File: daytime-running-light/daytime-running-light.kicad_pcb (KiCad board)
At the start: 2 copper layers, 47 parts, among them J1 Conn_01x01_Socket, J2 Conn_01x01_Socket, J3 Conn_01x01_Socket, J4 Conn_01x02_Socket, Q1 2N3904, Q2 2N3904, Q3 IRFZ44N, Q4 IRF9321, SW1 SW_SPST, SW2 SW_SPST, U1 L7812, U2 4069, U3 4001

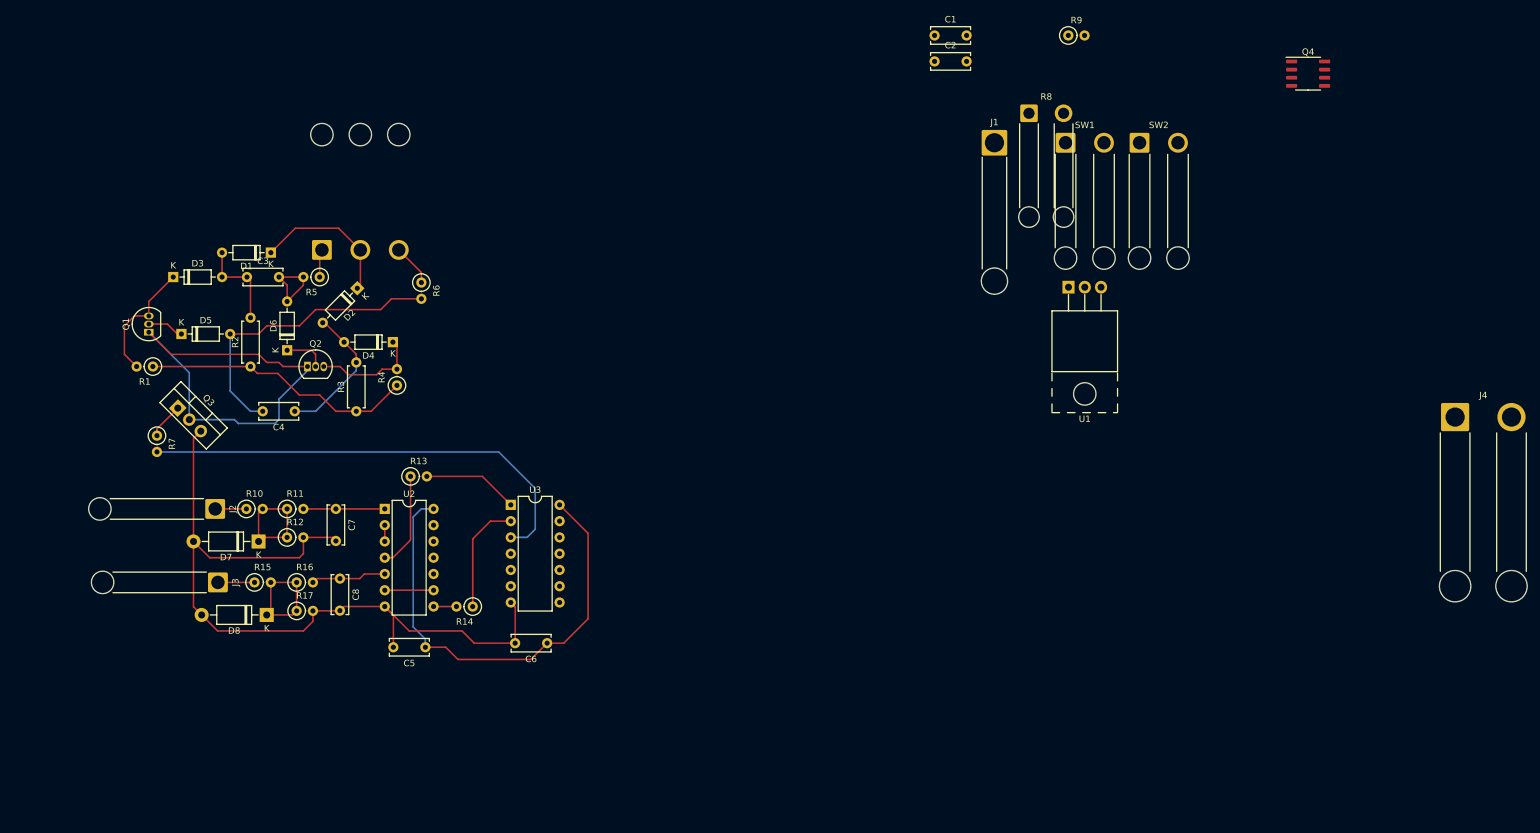
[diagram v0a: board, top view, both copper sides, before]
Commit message: [drl] Change daytime running light to use TLC555 timer.
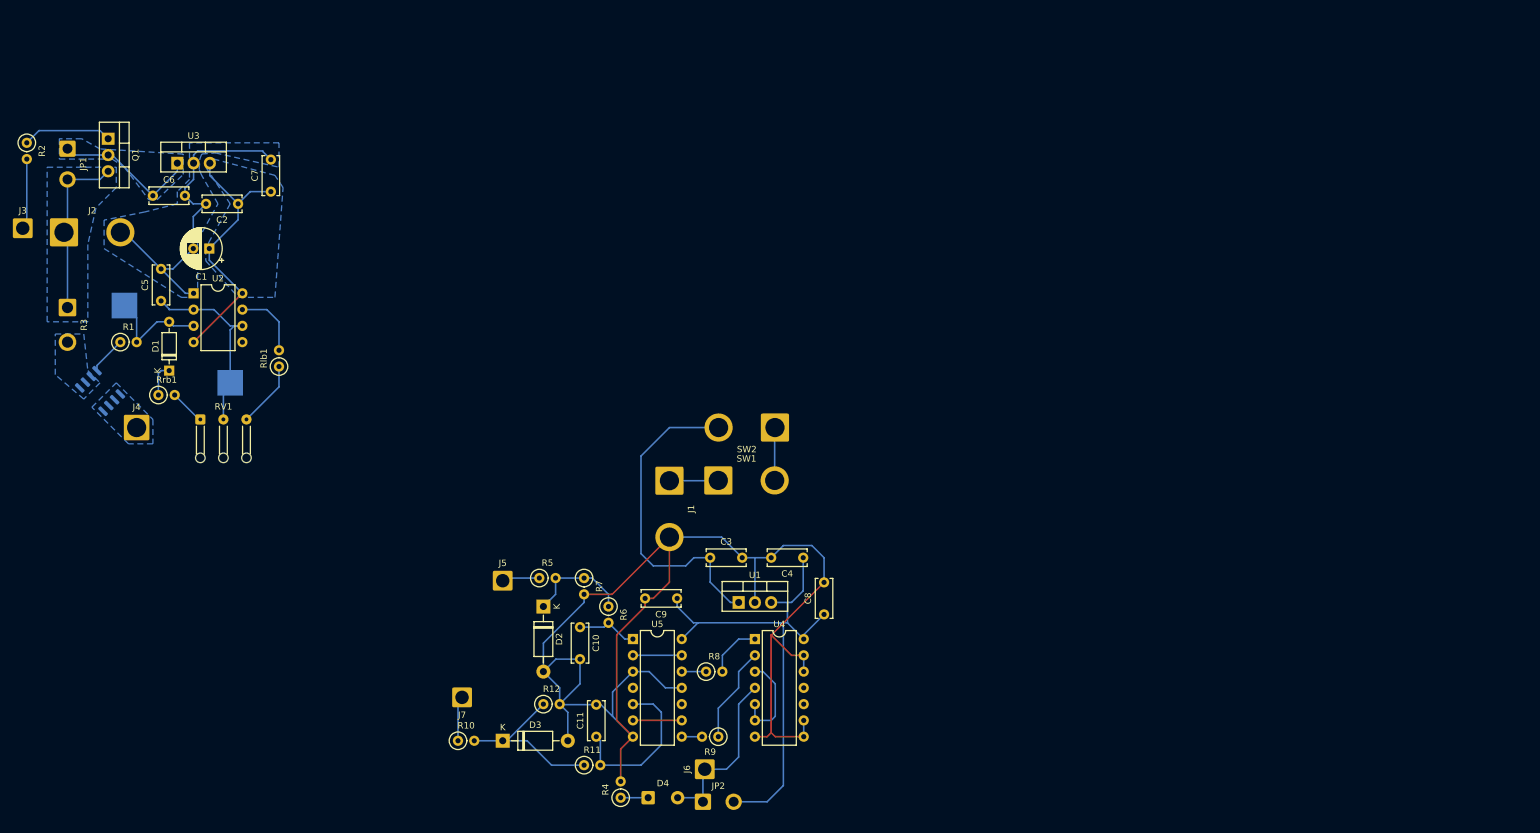
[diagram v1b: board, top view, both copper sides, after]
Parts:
- removed D5, D6: 1N4148, Diode_THT:D_DO-35_SOD27_P7.62mm_Horizontal
- removed D7: 1N47xxA, Diode_THT:D_DO-41_SOD81_P10.16mm_Horizontal
- removed D8: 1N4742A, Diode_THT:D_DO-41_SOD81_P10.16mm_Horizontal
- removed Q3: IRFZ44N, Package_TO_SOT_THT:TO-220-3_Vertical
- removed Q4: IRF9321, LIB:SO-8_3.9x4.9mm_P1.27mm
- removed R13, R14, R15: 1k, Resistor_THT:R_Axial_DIN0207_L6.3mm_D2.5mm_P2.54mm_Vertical
- removed R16: 47k, Resistor_THT:R_Axial_DIN0207_L6.3mm_D2.5mm_P2.54mm_Vertical
- removed R17: 100k, Resistor_THT:R_Axial_DIN0207_L6.3mm_D2.5mm_P2.54mm_Vertical
- added C10: 0.33uF, Capacitor_THT:C_Disc_D6.0mm_W2.5mm_P5.00mm, F.Cu at (127.0, 122.0)
- added C11: 0.33uF, Capacitor_THT:C_Disc_D6.0mm_W2.5mm_P5.00mm, F.Cu at (129.5, 139.1)
- added C9: 0.1uF, Capacitor_THT:C_Disc_D6.0mm_W2.5mm_P5.00mm, F.Cu at (142.2, 117.5)
- added J5: Conn_01x01_Socket, Connector_Wire:SolderWire-1.5sqmm_1x01_D1.7mm_OD3mm, F.Cu at (114.9, 114.7)
- added J6: Conn_01x01_Pin, Connector_Wire:SolderWire-1.5sqmm_1x01_D1.7mm_OD3mm, F.Cu at (146.5, 144.1)
- added J7: Conn_01x01_Socket, Connector_Wire:SolderWire-1.5sqmm_1x01_D1.7mm_OD3mm, F.Cu at (108.6, 132.9)
- added JP1: Jumper_2_Open, Connector_Wire:SolderWire-0.75sqmm_1x02_P4.8mm_D1.25mm_OD2.3mm, F.Cu at (47.0, 47.3)
- added JP2: Jumper_2_Open, Connector_Wire:SolderWire-0.75sqmm_1x02_P4.8mm_D1.25mm_OD2.3mm, F.Cu at (146.2, 149.2)
- added Rlb1: 1k, Resistor_THT:R_Axial_DIN0207_L6.3mm_D2.5mm_P2.54mm_Vertical, F.Cu at (80.0, 81.3)
- added Rrb1: 1k, Resistor_THT:R_Axial_DIN0207_L6.3mm_D2.5mm_P2.54mm_Vertical, F.Cu at (61.2, 85.7)
- added TPpwm1: TestPoint, TestPoint:TestPoint_Pad_4.0x4.0mm, B.Cu at (55.9, 71.8)
- added TPpwmC1: TestPoint, TestPoint:TestPoint_Pad_4.0x4.0mm, B.Cu at (72.4, 83.8)
- added U4: 4001, Package_DIP:DIP-14_W7.62mm, F.Cu at (154.3, 123.8)
- added U5: 4069, Package_DIP:DIP-14_W7.62mm, F.Cu at (135.3, 123.8)
- C1: value 0.33uF -> 2u; footprint Capacitor_THT:C_Disc_D6.0mm_W2.5mm_P5.00mm -> Capacitor_THT:CP_Radial_D6.3mm_P2.50mm
- C2: value 0.1uF -> 0.1u
- C3: value 10nF -> 0.33uF
- C4: value 10nF -> 0.1uF
- C5: value 0.1uF -> 33n
- C6: value 0.1uF -> 0.33uF
- C7, C8: value 0.33uF -> 0.1uF
- D1: value 1N4148 -> BAT42
- D2: value 1N4148 -> 1N47xxA; footprint Diode_THT:D_DO-35_SOD27_P7.62mm_Horizontal -> Diode_THT:D_DO-41_SOD81_P10.16mm_Horizontal
- D3: value 1N4148 -> 1N4742A; footprint Diode_THT:D_DO-35_SOD27_P7.62mm_Horizontal -> Diode_THT:D_DO-41_SOD81_P10.16mm_Horizontal
- D4: value 1N4148 -> LED; footprint Diode_THT:D_DO-35_SOD27_P7.62mm_Horizontal -> Connector_Wire:SolderWire-0.5sqmm_1x02_P4.6mm_D0.9mm_OD2.1mm
- J1: value Conn_01x01_Socket -> Conn_01x02_Socket; footprint Connector_Wire:SolderWire-2.5sqmm_1x01_D2.4mm_OD3.6mm_Relief -> Connector_Wire:SolderWire-2.5sqmm_1x02_P8.8mm_D2.4mm_OD4.4mm
- J2: value Conn_01x01_Socket -> Conn_01x02_Socket; footprint Connector_Wire:SolderWire-1.5sqmm_1x01_D1.7mm_OD3mm_Relief -> Connector_Wire:SolderWire-2.5sqmm_1x02_P8.8mm_D2.4mm_OD4.4mm
- J3: footprint Connector_Wire:SolderWire-1.5sqmm_1x01_D1.7mm_OD3mm_Relief -> Connector_Wire:SolderWire-1.5sqmm_1x01_D1.7mm_OD3mm
- J4: value Conn_01x02_Socket -> Conn_01x01_Socket; footprint Connector_Wire:SolderWire-2.5sqmm_1x02_P8.8mm_D2.4mm_OD4.4mm_Relief -> Connector_Wire:SolderWire-2.5sqmm_1x01_D2.4mm_OD3.6mm
- Q1: value 2N3904 -> IRF9540N; footprint Package_TO_SOT_THT:TO-92_Inline -> Package_TO_SOT_THT:TO-220-3_Vertical
- Q2: value 2N3904 -> IRF9321; footprint Package_TO_SOT_THT:TO-92_Inline -> LIB:SO-8_3.9x4.9mm_P1.27mm; moved to B.Cu
- R1: value 3.9k -> 100..1k
- R2: value 3.9k -> 100; footprint Resistor_THT:R_Axial_DIN0207_L6.3mm_D2.5mm_P7.62mm_Horizontal -> Resistor_THT:R_Axial_DIN0207_L6.3mm_D2.5mm_P2.54mm_Vertical
- R3: value 3.9k -> 0.2; footprint Resistor_THT:R_Axial_DIN0207_L6.3mm_D2.5mm_P7.62mm_Horizontal -> Connector_Wire:SolderWire-1sqmm_1x02_P5.4mm_D1.4mm_OD2.7mm
- R4: value 3.9k -> R
- R6: value 1k -> 47k
- R7: value 100 -> 100k
- R8: value 0.2 -> 1k; footprint Connector_Wire:SolderWire-1sqmm_1x02_P5.4mm_D1.4mm_OD2.7mm_Relief -> Resistor_THT:R_Axial_DIN0207_L6.3mm_D2.5mm_P2.54mm_Vertical
- R9: value 100 -> 1k
- RV1: value 100k -> R_Potentiometer; footprint Connector_Wire:SolderWire-1.5sqmm_1x03_P6mm_D1.7mm_OD3mm_Relief -> Connector_Wire:SolderWire-0.1sqmm_1x03_P3.6mm_D0.4mm_OD1mm_Relief; moved to F.Cu
- SW1, SW2: footprint Connector_Wire:SolderWire-1.5sqmm_1x02_P6mm_D1.7mm_OD3mm_Relief -> Connector_Wire:SolderWire-2.5sqmm_1x02_P8.8mm_D2.4mm_OD4.4mm
- U1: footprint Package_TO_SOT_THT:TO-220-3_Horizontal_TabUp -> Package_TO_SOT_THT:TO-220-3_Vertical
- U2: value 4069 -> NE555; footprint Package_DIP:DIP-14_W7.62mm -> Package_DIP:DIP-8_W7.62mm
- U3: value 4001 -> L7812; footprint Package_DIP:DIP-14_W7.62mm -> Package_TO_SOT_THT:TO-220-3_Vertical
- moved J4 205.8 mm to (57.8, 90.8)
- moved R9 122.3 mm to (148.6, 139.1), turned to 180 degrees
- moved C1 118.0 mm to (69.1, 62.9), turned to 180 degrees
- moved C2 111.0 mm to (73.6, 55.9), turned to 180 degrees
- moved R8 100.7 mm to (146.7, 128.9)
- moved C6 93.1 mm to (60.3, 54.6), turned to 0 degrees
- moved D3 88.8 mm to (114.9, 139.7)
- moved C3 84.5 mm to (147.3, 111.1)
- moved C4 82.6 mm to (161.8, 111.1)
- moved D4 81.5 mm to (137.6, 148.6), turned to 0 degrees
- moved C8 75.8 mm to (165.1, 120.0), turned to 90 degrees
- moved SW1 75.6 mm to (148.6, 99.1)
- moved U3 74.5 mm to (64.1, 49.5)
- moved R4 73.2 mm to (133.3, 148.6)
- moved J1 73.2 mm to (141.0, 99.1), turned to -90 degrees
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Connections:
- C1 pad 1: Net-(SW2-B) -> /VCC_STAB2
- C1 pad 2: GND -> GND2
- C2 pad 1: /VCC_STAB -> /VCC_STAB2
- C2 pad 2: GND -> GND2
- C3 pad 1: Net-(D1-A) -> Net-(SW2-B)
- C3 pad 2: Net-(D6-A) -> GND
- C4 pad 1: Net-(D2-A) -> /VCC_STAB
- C4 pad 2: Net-(D5-A) -> GND
- C5 pad 1: /VCC_STAB -> /U1_TR
- C5 pad 2: GND -> GND2
- C6 pad 1: /VCC_STAB -> Net-(JP1-A)
- C6 pad 2: GND -> GND2
- C7 pad 1: Net-(C7-Pad1) -> /VCC_STAB2
- C7 pad 2: GND -> GND2
- C8 pad 1: Net-(C8-Pad1) -> /VCC_STAB
- D2 pad 1: Net-(D1-K) -> Net-(D2-K)
- D2 pad 2: Net-(D2-A) -> GND
- D3 pad 1: /POWER_CONTROL -> Net-(D3-K)
- D3 pad 2: Net-(D1-A) -> GND
- D4 pad 2: Net-(D2-A) -> Net-(D4-A)
- J1 pad 1: Net-(J1-Pin_1) -> VCC
- J2 pad 1: /HEADLIGHT -> +12V
- J3 pad 1: /HIGHBEAM -> Net-(J3-Pin_1)
- J4 pad 1: VCC -> Net-(J4-Pin_1)
- Q1 pad 1: Net-(Q1-E) -> Net-(Q1-G)
- Q1 pad 2: Net-(D5-K) -> Net-(JP1-A)
- Q1 pad 3: /POWER_CONTROL -> +12V
- Q2 pad 1: Net-(Q1-E) -> Net-(J4-Pin_1)
- Q2 pad 2: Net-(D6-K) -> /POWER_CONTROL
- Q2 pad 3: Net-(D4-K) -> Net-(Q2-S)
- R1 pad 1: /VCC_STAB -> /POWER_CONTROL
- R1 pad 2: /POWER_CONTROL -> Net-(D1-A)
- R10 pad 1: /HEADLIGHT -> /HIGHBEAM
- R10 pad 2: Net-(D7-K) -> Net-(D3-K)
- R11 pad 1: Net-(D7-K) -> Net-(D3-K)
- R11 pad 2: Net-(C7-Pad1) -> Net-(C11-Pad1)
- R12 pad 1: Net-(D7-K) -> Net-(D3-K)
- R2 pad 1: /VCC_STAB -> Net-(Q1-G)
- R2 pad 2: Net-(D1-A) -> Net-(J3-Pin_1)
- R3 pad 1: /VCC_STAB -> +12V
- R3 pad 2: Net-(D2-A) -> Net-(Q2-S)
- R4 pad 1: /VCC_STAB -> Net-(D4-K)
- R4 pad 2: Net-(D4-K) -> GND
- R5 pad 1: Net-(R5-Pad1) -> /HEADLIGHT
- R5 pad 2: Net-(D6-A) -> Net-(D2-K)
- R6 pad 1: Net-(R6-Pad1) -> Net-(D2-K)
- R6 pad 2: Net-(D5-A) -> Net-(C10-Pad1)
- R7 pad 1: Net-(Q3-Pad1) -> Net-(D2-K)
- R7 pad 2: /ALLOW_POWER -> GND
- R8 pad 1: VCC -> Net-(R8-Pad1)
- R9 pad 1: /POWER_CONTROL -> Net-(R9-Pad1)
- RV1 pad 1: Net-(R5-Pad1) -> Net-(RV1-Pad1)
- RV1 pad 2: Net-(D1-K) -> /U1_TR
- RV1 pad 3: Net-(R6-Pad1) -> Net-(RV1-Pad3)
- U2 pad 1: Net-(C7-Pad1) -> GND2
- U2 pad 2: Net-(U2-Pad2) -> /U1_TR
- U2 pad 3: Net-(U2-Pad2) -> Net-(D1-A)
- U2 pad 4: Net-(R13-Pad1) -> /VCC_STAB2
- U2 pad 5: Net-(C8-Pad1) -> unconnected-(U2-CV-Pad5)
- U2 pad 6: Net-(U2-Pad6) -> /U1_TR
- U2 pad 7: GND -> /U1_DISCH
- U2 pad 8: Net-(R14-Pad2) -> /VCC_STAB2
- U3 pad 1: Net-(R13-Pad2) -> Net-(JP1-A)
- U3 pad 2: Net-(R14-Pad1) -> GND2
- U3 pad 3: /ALLOW_POWER -> /VCC_STAB2
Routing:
- net GND: track 124.4 -> 218.0 mm
- net /ALLOW_POWER: track 72.1 -> 0.00 mm
- net Net-(Q1-E): track 67.9 -> 0.00 mm
- net GND2: track 0.00 -> 53.2 mm
- net Net-(SW2-B): track 0.00 -> 50.9 mm
- net Net-(D5-A): track 47.4 -> 0.00 mm
- net /VCC_STAB2: track 0.00 -> 42.8 mm
- net /VCC_STAB: track 115.9 -> 80.5 mm
- net /U1_TR: track 0.00 -> 30.9 mm
- net Net-(D3-K): track 0.00 -> 27.4 mm
- net Net-(D4-A): track 0.00 -> 27.3 mm
- net +12V: track 0.00 -> 27.3 mm
- net Net-(C11-Pad1): track 0.00 -> 25.6 mm
- net Net-(JP1-A): track 0.00 -> 23.0 mm
- net Net-(D2-A): track 22.0 -> 0.00 mm
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- added copper zone on B.Cu, net +12V
- added copper zone on B.Cu, net /VCC_STAB2
- added copper zone on B.Cu, net GND2
- added copper zone on B.Cu, net Net-(J4-Pin_1)
- added copper zone on B.Cu, net Net-(JP1-A)
- added copper zone on B.Cu, net Net-(Q2-S)

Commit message: [drl] Update
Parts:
- moved SW2 30.5 mm to (134.1, 110.5), turned to 0 degrees
- moved J1 10.8 mm to (150.5, 104.1), turned to 0 degrees
- moved R5 10.4 mm to (114.3, 122.6)
- moved R10 9.44 mm to (114.9, 133.3), turned to -90 degrees
- moved J7 7.52 mm to (114.9, 128.9)
- moved SW1 6.82 mm to (143.4, 103.5), turned to 180 degrees
- moved R7 4.49 mm to (127.0, 118.7), turned to 90 degrees
- moved J5 2.76 mm to (114.9, 117.5)
- moved R6 0.90 mm to (132.1, 119.4)
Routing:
- net GND: track 218.0 -> 68.8 mm, vias 0 -> 4
- net /VCC_STAB: track 80.5 -> 42.1 mm, vias 0 -> 2
- net Net-(SW2-B): track 50.9 -> 14.3 mm
- net /U1_TR: track 30.9 -> 1.58 mm
- net Net-(U4-Pad3): track 14.6 -> 18.0 mm
- net /HIGHBEAM: track 7.04 -> 4.44 mm
- net Net-(C11-Pad1): track 25.6 -> 26.7 mm
- net Net-(SW1-B): track 6.37 -> 7.21 mm
- net Net-(D3-K): track 27.4 -> 26.8 mm
- net Net-(D2-K): track 16.4 -> 17.1 mm
- net /HEADLIGHT: track 5.89 -> 5.34 mm
- net Net-(C10-Pad1): track 9.59 -> 9.07 mm
- added copper zone on B.Cu, net /U1_TR
- added copper zone on B.Cu, net /VCC_STAB
- added copper zone on B.Cu, net GND

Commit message: [drl] Change schematic and PCB
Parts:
- added D5: 1.5KExxA, Diode_THT:D_DO-201AE_P15.24mm_Horizontal, F.Cu at (51.4, 98.4)
- added D6: 1N4148, Diode_THT:D_DO-35_SOD27_P7.62mm_Horizontal, F.Cu at (54.6, 88.9)
- added Q3: BC548, LIB:TO-92_HandSolder2, F.Cu at (72.4, 55.2)
- added Q4: BC548, LIB:TO-92_HandSolder2, F.Cu at (57.1, 72.4)
- added Q5: BC548, Package_TO_SOT_THT:TO-92_HandSolder, F.Cu at (61.0, 82.9)
- added R13: 100, Resistor_THT:R_Axial_DIN0207_L6.3mm_D2.5mm_P2.54mm_Vertical, F.Cu at (150.9, 144.1)
- added R14: 10k..100k, Resistor_THT:R_Axial_DIN0207_L6.3mm_D2.5mm_P2.54mm_Vertical, F.Cu at (76.2, 50.2)
- added R15: 10k..100k, Resistor_THT:R_Axial_DIN0207_L6.3mm_D2.5mm_P2.54mm_Vertical, F.Cu at (52.2, 76.4)
- added R16: 100, Resistor_THT:R_Axial_DIN0207_L6.3mm_D2.5mm_P2.54mm_Vertical, F.Cu at (58.6, 76.4)
- added R17: 10k, Resistor_THT:R_Axial_DIN0207_L6.3mm_D2.5mm_P2.54mm_Vertical, F.Cu at (55.9, 84.5)
- C1: value 2u -> 0.1u
- Q1, U3: footprint Package_TO_SOT_THT:TO-220-3_Vertical -> LIB:TO-220-3_Vertical-mod
- R1: value 100..1k -> 10k
- R2: value 100 -> 10k
- RV1: value R_Potentiometer -> 51k
- Rlb1: value 1k -> 51k
- U2: value NE555 -> TLC555xP
- moved J3 33.0 mm to (69.8, 45.7)
- moved C6 32.3 mm to (92.1, 48.9), turned to 180 degrees
- moved U3 28.5 mm to (92.1, 54.6), turned to -90 degrees
- moved R2 23.2 mm to (63.7, 48.3), turned to 0 degrees
- moved TPpwm1 22.5 mm to (73.0, 86.4)
- moved C7 17.5 mm to (92.1, 65.4), turned to 180 degrees
- moved RV1 15.2 mm to (79.8, 80.4)
- moved R3 15.1 mm to (49.0, 87.0)
- moved Q2 14.8 mm to (59.7, 97.8), turned to 0 degrees
- moved Rrb1 14.0 mm to (74.1, 80.2)
- moved TPpwmC1 14.0 mm to (83.2, 92.7)
- moved C1 13.7 mm to (82.5, 60.3)
- moved C2 10.9 mm to (83.8, 52.1)
- moved J4 10.3 mm to (67.9, 92.7)
- moved Q1 9.92 mm to (60.4, 52.7)
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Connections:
- net Net-(Q1-G) renamed /ALLOW_POWER_ON
- D1 pad 2: Net-(D1-A) -> /POWER_CONTROL
- J6 pad 1: Net-(D4-A) -> Net-(J6-Pin_1)
- Q2 pad 2: /POWER_CONTROL -> Net-(D6-A)
- R1 pad 1: /POWER_CONTROL -> Net-(Q4-B)
- R1 pad 2: Net-(D1-A) -> /POWER_CONTROL
- TPpwm1 pad 1: Net-(D1-A) -> /POWER_CONTROL
- U2 pad 3: Net-(D1-A) -> /POWER_CONTROL
- U2 pad 4: /VCC_STAB2 -> Net-(Q3-C)
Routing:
- net GND2: track 53.2 -> 11.9 mm
- net Net-(JP1-A): track 23.0 -> 63.8 mm
- net /U1_TR: track 1.58 -> 38.1 mm
- net +12V: track 27.3 -> 2.01 mm
- net Net-(Q3-C): track 0.00 -> 25.2 mm
- net Net-(D6-K): track 0.00 -> 21.8 mm
- net Net-(D5-A1): track 0.00 -> 19.9 mm
- net GND: track 68.8 -> 88.0 mm, vias 4 -> 2
- net Net-(D6-A): track 0.00 -> 17.5 mm
- net Net-(D1-A): track 17.0 -> 0.00 mm
- net Net-(SW2-B): track 14.3 -> 0.90 mm
- net /POWER_CONTROL_INV: track 0.00 -> 8.36 mm
- net VCC: track 7.34 -> 0.90 mm
- net Net-(SW1-B): track 7.21 -> 0.77 mm
- net Net-(J3-Pin_1): track 11.1 -> 4.64 mm
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- added copper zone on B.Cu, net /POWER_CONTROL
- added copper zone on B.Cu, net Net-(SW1-B)
- added copper zone on B.Cu, net Net-(SW2-B)
- added copper zone on B.Cu, net VCC
- removed copper zone on B.Cu, net /U1_TR
- removed copper zone on B.Cu, net /VCC_STAB2
- removed copper zone on B.Cu, net Net-(JP1-A)
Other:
- board outline added: 130.2 x 112.4 mm

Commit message: [drl] Change schematic and PCB
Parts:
- added R18: R, Resistor_THT:R_Axial_DIN0207_L6.3mm_D2.5mm_P2.54mm_Vertical, F.Cu at (141.0, 148.6)
- moved R4 32.4 mm to (165.7, 148.4)
- moved D4 23.2 mm to (160.8, 148.6), turned to 180 degrees
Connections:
- JP2 pad 1: Net-(D4-A) -> Net-(JP2-A)
- JP2 pad 2: /VCC_STAB -> Net-(D4-A)
- R4 pad 2: GND -> /VCC_STAB
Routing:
- net /VCC_STAB: track 42.1 -> 27.2 mm
- net GND2: track 11.9 -> 13.2 mm
- net GND: track 88.0 -> 89.0 mm
- net Net-(JP2-A): track 0.00 -> 1.00 mm
- net Net-(D4-K): track 4.29 -> 5.02 mm
- net Net-(D4-A): track 25.4 -> 24.7 mm
- added copper zone on B.Cu, net Net-(JP2-A)

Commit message: [drl] Change schematic and PCB
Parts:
- D4: footprint Connector_Wire:SolderWire-0.5sqmm_1x02_P4.6mm_D0.9mm_OD2.1mm -> LED_THT:LED_D5.0mm
- moved R4 22.6 mm to (167.7, 125.8), turned to 135 degrees
- moved D4 17.7 mm to (165.1, 131.4), turned to 0 degrees
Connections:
- JP2 pad 2: Net-(D4-A) -> Net-(JP2-B)
- R13 pad 1: Net-(D4-A) -> Net-(JP2-B)
- R4 pad 1: Net-(D4-K) -> Net-(D4-A)
- U4 pad 11: unconnected-(U4-Pad11) -> Net-(D4-K)
- U4 pad 12: GND -> Net-(U4-Pad12)
- U4 pad 13: GND -> Net-(U4-Pad12)
- U4 pad 3: Net-(U4-Pad3) -> Net-(U4-Pad12)
- U4 pad 4: Net-(D4-A) -> Net-(JP2-B)
- U4 pad 5: Net-(U4-Pad3) -> Net-(U4-Pad12)
- U4 pad 6: Net-(U4-Pad3) -> Net-(U4-Pad12)
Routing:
- net Net-(U4-Pad12): track 0.00 -> 28.2 mm
- net /VCC_STAB: track 27.2 -> 1.87 mm, vias 2 -> 0
- net Net-(JP2-B): track 0.00 -> 19.2 mm
- net Net-(D4-A): track 24.7 -> 5.66 mm
- net Net-(U4-Pad3): track 18.0 -> 0.00 mm
- net GND: track 89.0 -> 86.4 mm
- net Net-(D4-K): track 5.02 -> 3.17 mm
- net /VCC_STAB2: track 39.2 -> 38.3 mm, vias 0 -> 1
- added copper zone on B.Cu, net /VCC_STAB2
